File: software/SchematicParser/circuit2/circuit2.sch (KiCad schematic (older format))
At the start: 17 parts, among them Q1 Transistor, SW1 SwitchPush, U1-8 8pinChip, U2-6 6pinRelay, U3-16 16pinChip

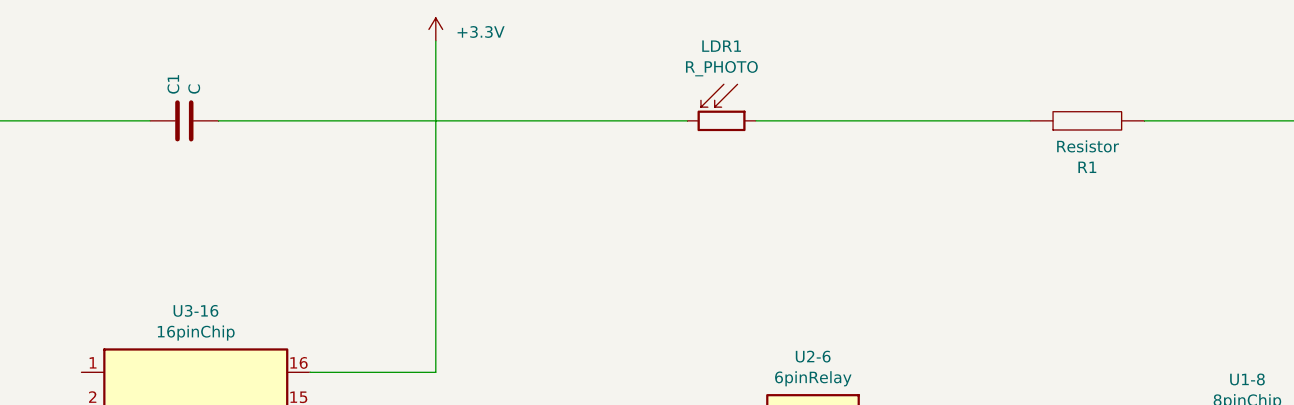
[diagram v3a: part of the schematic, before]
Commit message: Recover initial position if the user changes mode with disconnected components
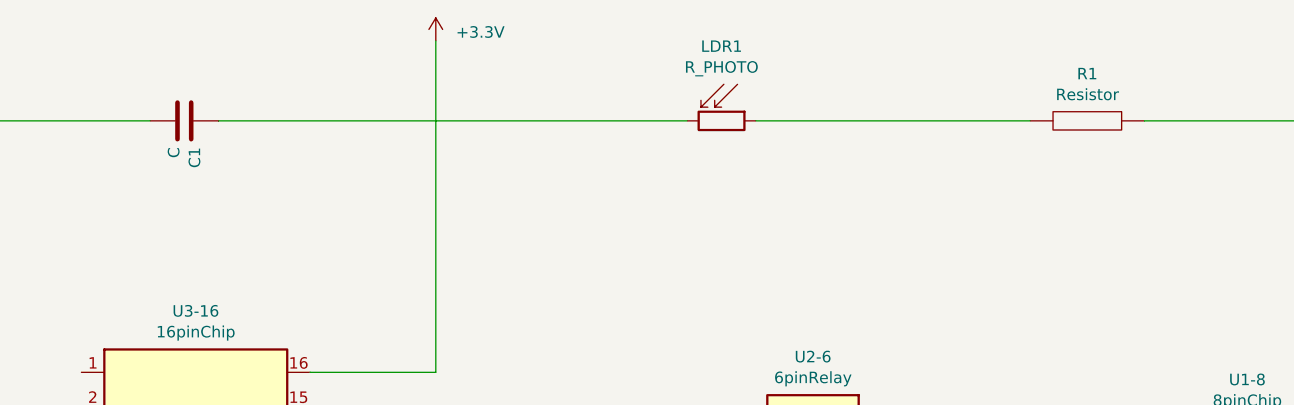
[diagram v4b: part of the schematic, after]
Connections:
- net at SP1.1: now also R1.1; no longer R1.2
- net at LDR1.1: now also R1.2; no longer R1.1
- net at LDR1.2: now also C1.1; no longer C1.2
- net at U3-16.2: now also C1.2; no longer C1.1
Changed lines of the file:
@@
 F 3 "~" H 1950 2050 50  0001 C CNN
 	1    1950 2050
-	0    -1   -1   0
+	0    1    1    0
 $EndComp
 $Comp
@@
 F 3 "~" H 5900 2050 50  0001 C CNN
 	1    5900 2050
-	0    -1   -1   0
+	0    1    1    0
 $EndComp
 $Comp
